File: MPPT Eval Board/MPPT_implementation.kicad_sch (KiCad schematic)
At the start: 3 parts

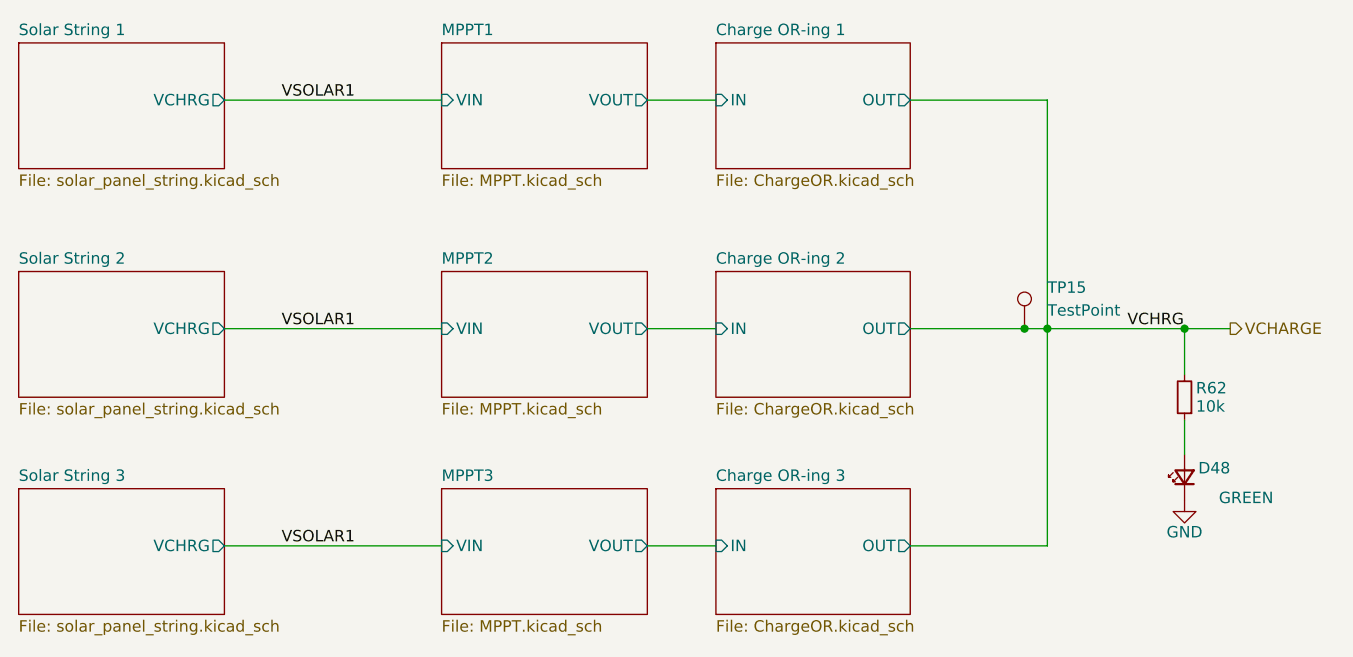
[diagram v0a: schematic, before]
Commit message: Added I2C pullups and board ready for layout
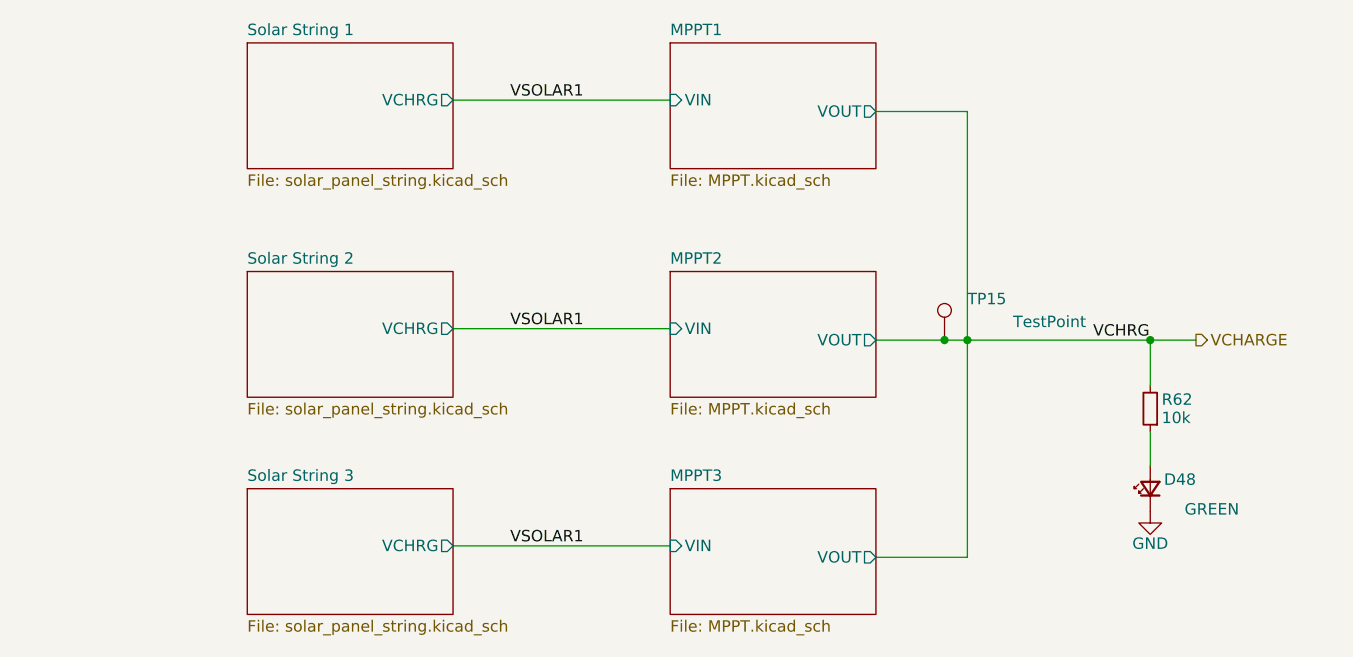
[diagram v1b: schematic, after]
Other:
- removed sheet Charge OR-ing 1
- removed sheet Charge OR-ing 2
- removed sheet Charge OR-ing 3
- moved on the sheet: D48, R62, TP15
